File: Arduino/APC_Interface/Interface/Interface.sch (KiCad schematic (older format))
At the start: 8 parts, among them J1 UPS_Interface, Q1 PN100, U1 LEOSTICK_SHIELD

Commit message: Update schematic and create PCB layout
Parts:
- added Q2: PN100, Package_TO_SOT_THT:TO-92Flat, symbol Transistor_BJT:PN2222A
- added R6: 4.7K, Resistor_THT:R_Axial_DIN0207_L6.3mm_D2.5mm_P7.62mm_Horizontal, symbol Device:R
- J1: footprint (none) -> Connector_Dsub:DSUB-9_Male_Horizontal_P2.77x2.84mm_EdgePinOffset7.70mm_Housed_MountingHolesOffset9.12mm
- Q1: footprint (none) -> Package_TO_SOT_THT:TO-92Flat; symbol Freetronics:TRANSISTOR_NPN -> Transistor_BJT:PN2222A
- R1, R2, R3, R4, R5: footprint (none) -> Resistor_THT:R_Axial_DIN0207_L6.3mm_D2.5mm_P7.62mm_Horizontal
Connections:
- net GND: now also Q2.1 (E); no longer R1.1, R2.1, R3.1
- net at U1.12 (D12): now also Q2.2 (B); no longer J1.7
- net at U1.18 (5V): now also Q1.3 (C), R1.1, R2.1, R3.1; no longer Q1.C
- net at R5.1: now also Q1.1 (E); no longer Q1.E
- net at R4.2: now also Q1.2 (B); no longer Q1.B
- new net: J1.7, R6.2
- new net: Q2.3 (C), R6.1
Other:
- moved on the sheet: J1, R1, R2, R3, R4, R5, U1

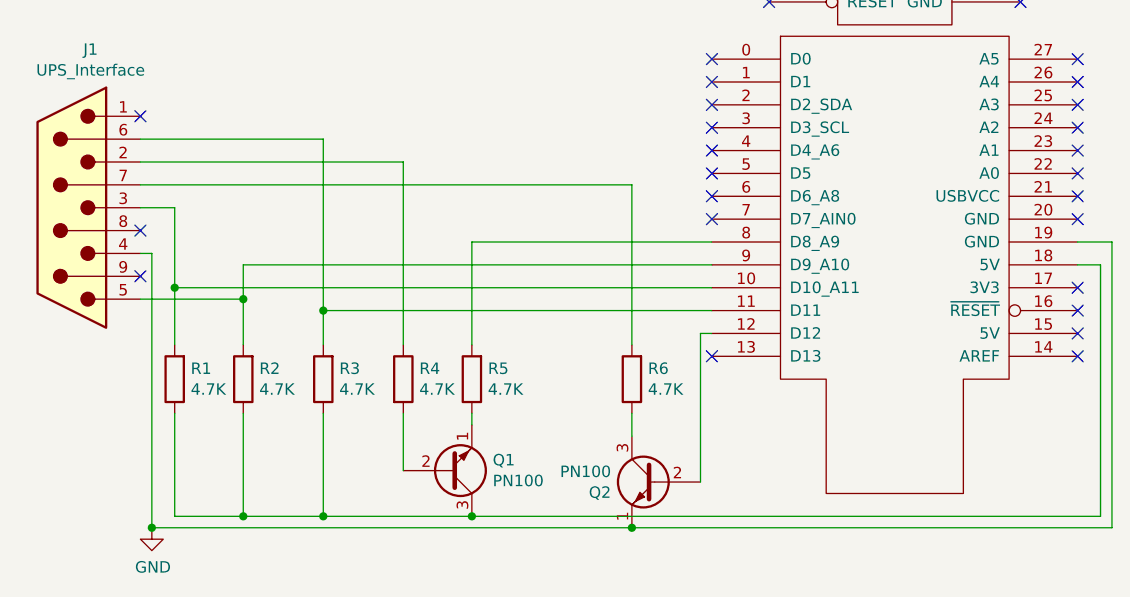
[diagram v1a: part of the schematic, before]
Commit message: Updated schematic & layout, floating ground
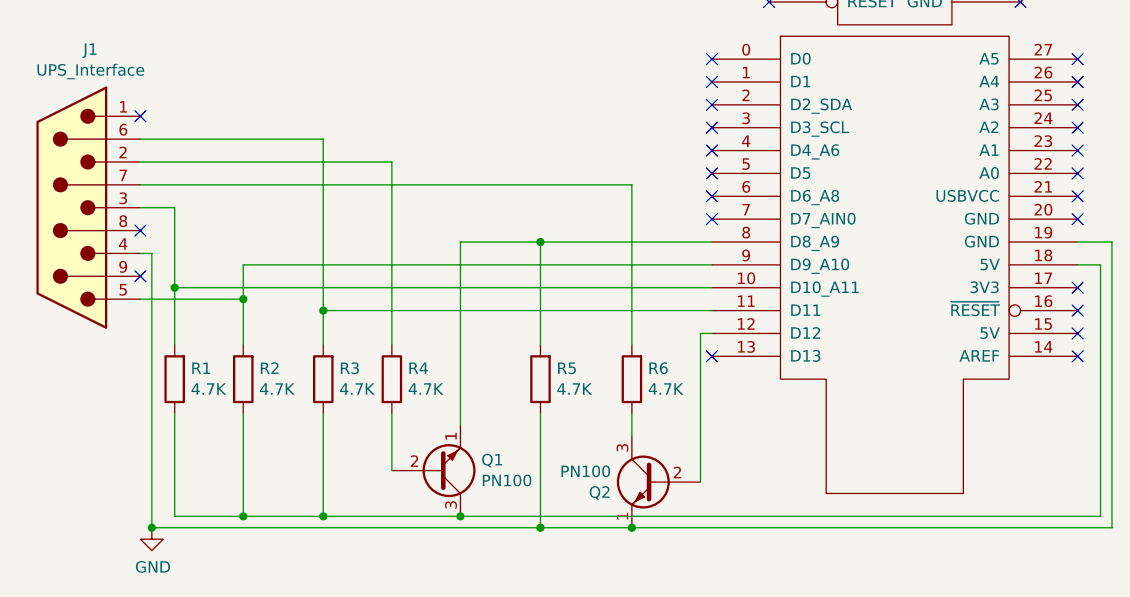
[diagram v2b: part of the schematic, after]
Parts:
- R1, R2, R3, R4, R5, R6: footprint Resistor_THT:R_Axial_DIN0207_L6.3mm_D2.5mm_P7.62mm_Horizontal -> Resistor_THT:R_Axial_DIN0207_L6.3mm_D2.5mm_P10.16mm_Horizontal
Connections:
- net GND: now also R5.1
- net at R5.2, U1.8 (D8_A9): now also Q1.1 (E)
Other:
- moved on the sheet: Q1, R4, R5
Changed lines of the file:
@@
 F 0 "R2" H 1430 2554 50  0000 R CNN
 F 1 "4.7K" H 1430 2645 50  0000 R CNN
-F 2 "Resistor_THT:R_Axial_DIN0207_L6.3mm_D2.5mm_P7.62mm_Horizontal" V 1430 2600 50  0001 C CNN
+F 2 "Resistor_THT:R_Axial_DIN0207_L6.3mm_D2.5mm_P10.16mm_Horizontal" V 1430 2600 50  0001 C CNN
 F 3 "~" H 1500 2600 50  0001 C CNN
 	1    1500 2600
@@
 L Device:R R5
 U 1 1 5E51218F
-P 2500 2600
-F 0 "R5" H 2430 2554 50  0000 R CNN
-F 1 "4.7K" H 2430 2645 50  0000 R CNN
-F 2 "Resistor_THT:R_Axial_DIN0207_L6.3mm_D2.5mm_P7.62mm_Horizontal" V 2430 2600 50  0001 C CNN
-F 3 "~" H 2500 2600 50  0001 C CNN
-	1    2500 2600
+P 2800 2600
+F 0 "R5" H 2730 2554 50  0000 R CNN
+F 1 "4.7K" H 2730 2645 50  0000 R CNN
+F 2 "Resistor_THT:R_Axial_DIN0207_L6.3mm_D2.5mm_P10.16mm_Horizontal" V 2730 2600 50  0001 C CNN
+F 3 "~" H 2800 2600 50  0001 C CNN
+	1    2800 2600
 	-1   0    0    1
 $EndComp
@@
 L Device:R R4
 U 1 1 5E51263D
-P 2200 2600
-F 0 "R4" H 2270 2646 50  0000 L CNN
-F 1 "4.7K" H 2270 2555 50  0000 L CNN
-F 2 "Resistor_THT:R_Axial_DIN0207_L6.3mm_D2.5mm_P7.62mm_Horizontal" V 2130 2600 50  0001 C CNN
-F 3 "~" H 2200 2600 50  0001 C CNN
-	1    2200 2600
+P 2150 2600
+F 0 "R4" H 2220 2646 50  0000 L CNN
+F 1 "4.7K" H 2220 2555 50  0000 L CNN
+F 2 "Resistor_THT:R_Axial_DIN0207_L6.3mm_D2.5mm_P10.16mm_Horizontal" V 2080 2600 50  0001 C CNN
+F 3 "~" H 2150 2600 50  0001 C CNN
+	1    2150 2600
 	1    0    0    -1
 $EndComp
@@
 F 0 "R1" H 1130 2554 50  0000 R CNN
 F 1 "4.7K" H 1130 2645 50  0000 R CNN
-F 2 "Resistor_THT:R_Axial_DIN0207_L6.3mm_D2.5mm_P7.62mm_Horizontal" V 1130 2600 50  0001 C CNN
+F 2 "Resistor_THT:R_Axial_DIN0207_L6.3mm_D2.5mm_P10.16mm_Horizontal" V 1130 2600 50  0001 C CNN
 F 3 "~" H 1200 2600 50  0001 C CNN
 	1    1200 2600
@@
 F 0 "R3" H 1780 2554 50  0000 R CNN
 F 1 "4.7K" H 1780 2645 50  0000 R CNN
-F 2 "Resistor_THT:R_Axial_DIN0207_L6.3mm_D2.5mm_P7.62mm_Horizontal" V 1780 2600 50  0001 C CNN
+F 2 "Resistor_THT:R_Axial_DIN0207_L6.3mm_D2.5mm_P10.16mm_Horizontal" V 1780 2600 50  0001 C CNN
 F 3 "~" H 1850 2600 50  0001 C CNN
 	1    1850 2600
@@
 	1500 2100 1500 2250
 Wire Wire Line
-	1850 2300 1850 2450
-Wire Wire Line
 	1050 1550 1850 1550
-Wire Wire Line
-	1850 1550 1850 2300
-Connection ~ 1850 2300
 $Comp
 L power:GND #PWR0101
@@
 L Transistor_BJT:PN2222A Q1
 U 1 1 5E54FE29
-P 2400 3000
-F 0 "Q1" H 2591 2954 50  0000 L CNN
-F 1 "PN100" H 2591 3045 50  0000 L CNN
-F 2 "Package_TO_SOT_THT:TO-92Flat" H 2500 4200 60  0001 C CNN
-F 3 "https://www.futurlec.com/Transistors/PN100.shtml" H 2400 3000 60  0001 C CNN
-	1    2400 3000
+P 2350 3000
+F 0 "Q1" H 2541 2954 50  0000 L CNN
+F 1 "PN100" H 2541 3045 50  0000 L CNN
+F 2 "Package_TO_SOT_THT:TO-92Flat" H 2450 4200 60  0001 C CNN
+F 3 "https://www.futurlec.com/Transistors/PN100.shtml" H 2350 3000 60  0001 C CNN
+	1    2350 3000
 	1    0    0    1
 $EndComp
 Wire Wire Line
-	2200 1650 2200 2450
-Wire Wire Line
-	1050 1650 2200 1650
-Wire Wire Line
-	2200 2750 2200 3000
+	2150 1650 2150 2450
+Wire Wire Line
+	1050 1650 2150 1650
+Wire Wire Line
+	2150 2750 2150 3000
 Wire Wire Line
 	5250 3200 5250 2100
-Wire Wire Line
-	1200 1850 1200 2200
-Connection ~ 1200 2200
-Wire Wire Line
-	1200 2200 1200 2450
-Wire Wire Line
-	2500 2800 2500 2750
-Wire Wire Line
-	2500 2000 2500 2450
 Wire Wire Line
 	1050 2250 1500 2250
@@
 NoConn ~ 1050 2150
 Wire Wire Line
-	2500 3200 1850 3200
+	2450 3200 1850 3200
 Wire Wire Line
 	1200 3200 1200 2750
-Connection ~ 2500 3200
+Connection ~ 2450 3200
 Wire Wire Line
 	1500 2750 1500 3200
@@
 	1850 3200 1500 3200
 Wire Wire Line
-	2500 3200 5250 3200
+	2450 3200 5250 3200
 Wire Wire Line
 	3200 1750 1050 1750
@@
 	3550 2400 3500 2400
 NoConn ~ 5150 1800
-Wire Wire Line
-	3550 2300 1850 2300
 NoConn ~ 5150 1900
-Wire Wire Line
-	3550 2200 1200 2200
-Wire Wire Line
-	3550 2100 1500 2100
-Wire Wire Line
-	3550 2000 2500 2000
 NoConn ~ 3550 1900
 NoConn ~ 3550 1800
@@
 	-1   0    0    -1
 $EndComp
-Wire Wire Line
-	1100 3250 3200 3250
 Connection ~ 3200 3250
 Wire Wire Line
@@
 F 0 "R6" H 3130 2554 50  0000 R CNN
 F 1 "4.7K" H 3130 2645 50  0000 R CNN
-F 2 "Resistor_THT:R_Axial_DIN0207_L6.3mm_D2.5mm_P7.62mm_Horizontal" V 3130 2600 50  0001 C CNN
+F 2 "Resistor_THT:R_Axial_DIN0207_L6.3mm_D2.5mm_P10.16mm_Horizontal" V 3130 2600 50  0001 C CNN
 F 3 "~" H 3200 2600 50  0001 C CNN
 	1    3200 2600
@@
 Wire Wire Line
 	3200 2450 3200 1750
+Wire Wire Line
+	1100 3250 2800 3250
+Connection ~ 1200 2200
+Wire Wire Line
+	1200 2200 1200 2450
+Wire Wire Line
+	1200 1850 1200 2200
+Connection ~ 1850 2300
+Wire Wire Line
+	1850 1550 1850 2300
+Wire Wire Line
+	1850 2300 1850 2450
+Wire Wire Line
+	3550 2100 1500 2100
+Wire Wire Line
+	3550 2200 1200 2200
+Wire Wire Line
+	3550 2300 1850 2300
+Wire Wire Line
+	2450 2000 2800 2000
+Wire Wire Line
+	2450 2000 2450 2800
+Wire Wire Line
+	2800 2450 2800 2000
+Connection ~ 2800 2000
+Wire Wire Line
+	2800 2000 3550 2000
+Wire Wire Line
+	2800 2750 2800 3250
+Connection ~ 2800 3250
+Wire Wire Line
+	2800 3250 3200 3250
 $EndSCHEMATC
